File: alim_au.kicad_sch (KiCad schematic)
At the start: 34 parts, among them U1 AMS1117-3.3

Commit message: Correction orientation conn alim
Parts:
- C1, C?: LCSC (none) -> C440198
- C2: LCSC (none) -> C1588
- C?: LCSC (none) -> C45783
- C? (x2): LCSC (none) -> C14663
- C?: LCSC (none) -> C1620
- D20, D?: LCSC (none) -> C2286
- D? (x2): JLCPCB C191023 -> (none); LCSC (none) -> C191023
- D?: LCSC (none) -> C330388
- D?: LCSC (none) -> C603316
- Q? (x2): LCSC (none) -> C20917
- Q?: LCSC (none) -> C435954
- R30, R?: LCSC (none) -> C23162
- R34, R? (x5): LCSC (none) -> C25804
- R? (x2): LCSC (none) -> C25803
- R?: LCSC (none) -> C185324
- U1: LCSC (none) -> C7376
- U?: LCSC (none) -> C473914

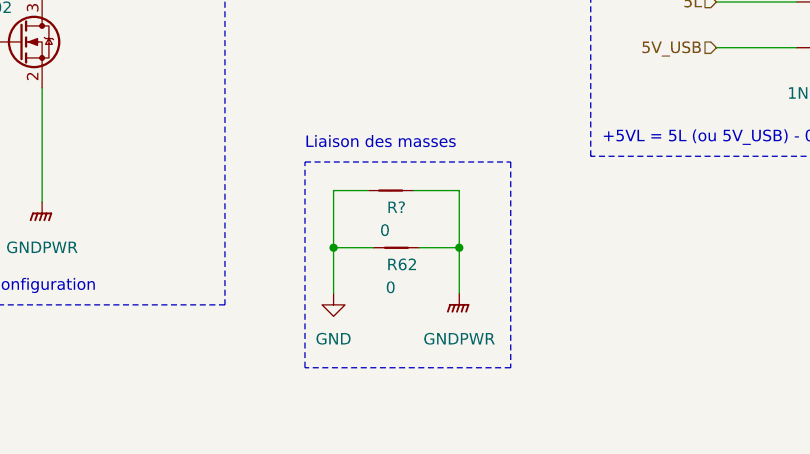
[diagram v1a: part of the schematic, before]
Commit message: added generic JLCPCB switch for reset and gnd netTie
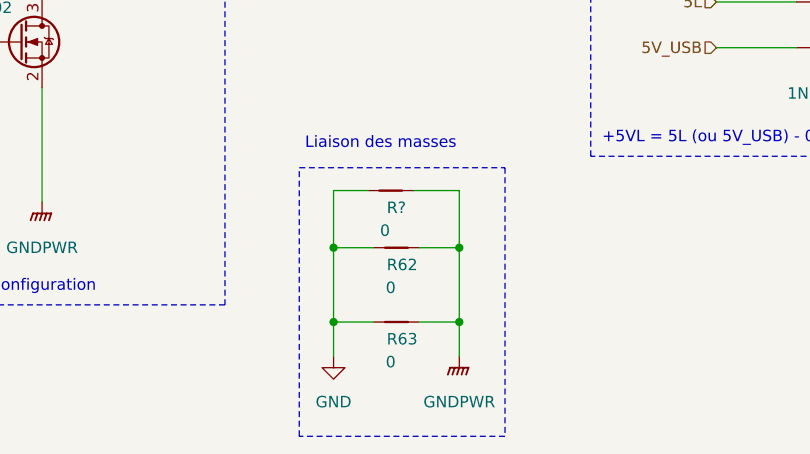
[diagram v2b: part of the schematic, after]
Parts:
- added R63: 0, NetTie:NetTie-2_SMD_Pad0.5mm, symbol Device:NetTie_2
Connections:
- net GND: now also R63.2
- net GNDPWR: now also R63.1
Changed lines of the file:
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@@
 	)
 	(junction
+		(at 124.46 162.56)
+		(diameter 0)
+		(color 0 0 0 0)
+	)
+	(junction
 		(at 126.365 67.31)
 		(diameter 0)
@@
 	)
 	(junction
+		(at 138.43 162.56)
+		(diameter 0)
+		(color 0 0 0 0)
+	)
+	(junction
 		(at 238.125 135.255)
 		(diameter 0)
@@
 	(wire
 		(pts
-			(xy 124.46 154.305) (xy 124.46 159.385)
+			(xy 124.46 154.305) (xy 124.46 162.56)
 		)
 		(stroke
@@
 	(wire
 		(pts
+			(xy 138.43 162.56) (xy 138.43 166.37)
+		)
+		(stroke
+			(width 0.5)
+			(type default)
+			(color 0 0 0 1)
+		)
+	)
+	(wire
+		(pts
 			(xy 243.84 60.325) (xy 250.825 60.325)
 		)
@@
 	(wire
 		(pts
+			(xy 124.46 162.56) (xy 128.905 162.56)
+		)
+		(stroke
+			(width 0)
+			(type default)
+		)
+	)
+	(wire
+		(pts
 			(xy 66.04 63.5) (xy 66.04 67.31)
 		)
@@
 	(wire
 		(pts
+			(xy 133.985 162.56) (xy 138.43 162.56)
+		)
+		(stroke
+			(width 0.5)
+			(type default)
+			(color 0 0 0 1)
+		)
+	)
+	(wire
+		(pts
 			(xy 80.645 77.47) (xy 70.485 77.47)
 		)
@@
 	(wire
 		(pts
+			(xy 124.46 162.56) (xy 124.46 166.37)
+		)
+		(stroke
+			(width 0)
+			(type default)
+		)
+	)
+	(wire
+		(pts
 			(xy 126.365 67.31) (xy 126.365 71.12)
 		)
@@
 	(wire
 		(pts
-			(xy 138.43 154.305) (xy 138.43 159.385)
+			(xy 138.43 154.305) (xy 138.43 162.56)
 		)
 		(stroke
@@
 	)
 	(rectangle
-		(start 121.285 144.78)
-		(end 144.145 167.64)
+		(start 120.65 145.415)
+		(end 143.51 175.26)
 		(stroke
 			(width 0)
@@
 	(symbol
 		(lib_id "power:GNDPWR")
-		(at 138.43 159.385 0)
+		(at 138.43 166.37 0)
 		(unit 1)
 		(exclude_from_sim no)
@@
 		(dnp no)
 		(property "Reference" "#PWR73"
-			(at 138.43 164.465 0)
+			(at 138.43 171.45 0)
 			(effects
 				(font
@@
 		)
 		(property "Value" "GNDPWR"
-			(at 138.43 164.465 0)
+			(at 138.43 171.45 0)
 			(effects
 				(font
@@
 		)
 		(property "Footprint" ""
-			(at 138.43 160.655 0)
+			(at 138.43 167.64 0)
 			(effects
 				(font
@@
 		)
 		(property "Datasheet" ""
-			(at 138.43 160.655 0)
+			(at 138.43 167.64 0)
 			(effects
 				(font
@@
 		)
 		(property "Description" ""
-			(at 138.43 159.385 0)
+			(at 138.43 166.37 0)
 			(effects
 				(font
@@
 	(symbol
 		(lib_id "power:GND")
-		(at 124.46 159.385 0)
+		(at 124.46 166.37 0)
 		(unit 1)
 		(exclude_from_sim no)
@@
 		(fields_autoplaced yes)
 		(property "Reference" "#PWR56"
-			(at 124.46 165.735 0)
+			(at 124.46 172.72 0)
 			(effects
 				(font
@@
 		)
 		(property "Value" "GND"
-			(at 124.46 164.465 0)
+			(at 124.46 171.45 0)
 			(effects
 				(font
@@
 		)
 		(property "Footprint" ""
-			(at 124.46 159.385 0)
+			(at 124.46 166.37 0)
 			(effects
 				(font
@@
 		)
 		(property "Datasheet" ""
-			(at 124.46 159.385 0)
+			(at 124.46 166.37 0)
 			(effects
 				(font
@@
 		)
 		(property "Description" ""
-			(at 124.46 159.385 0)
+			(at 124.46 166.37 0)
 			(effects
 				(font
@@
 					(unit 1)
 				)
+			)
+		)
+	)
+	(symbol
+		(lib_id "Device:NetTie_2")
+		(at 131.445 162.56 180)
+		(unit 1)
+		(exclude_from_sim no)
+		(in_bom no)
+		(on_board yes)
+		(dnp no)
+		(property "Reference" "R63"
+			(at 132.08 164.465 0)
+			(effects
+				(font
+					(size 1.27 1.27)
+				)
+			)
+		)
+		(property "Value" "0"
+			(at 130.81 167.005 0)
+			(effects
+				(font
+					(size 1.27 1.27)
+				)
+			)
+		)
+		(property "Footprint" "NetTie:NetTie-2_SMD_Pad0.5mm"
+			(at 131.445 162.56 0)
+			(effects
+				(font
+					(size 1.27 1.27)
+				)
+				(hide yes)
+			)
+		)
+		(property "Datasheet" "~"
+			(at 131.445 162.56 0)
+			(effects
+				(font
+					(size 1.27 1.27)
+				)
+				(hide yes)
+			)
+		)
+		(property "Description" "Net tie, 2 pins"
+			(at 131.445 162.56 0)
+			(effects
+				(font
+					(size 1.27 1.27)
+				)
+				(hide yes)
+			)
+		)
+		(pin "1"
+		)
+		(pin "2"
+		)
+		(instances
+			(project "12v-actuators-pcb"
+				(path "/d0b6cc72-ff07-4f5e-a148-04b65c86a715/a9998e65-7bac-4337-98c8-7de7c845405f"
+					(reference "R63")
+					(unit 1)
+				)

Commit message: corrrection footprint trim, ajout R64, config JLCPCB ASSY, fin panelisation (TODO: revue et cmd)
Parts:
- added R64: 13k, Resistor_SMD:R_0603_1608Metric, symbol Device:R_Small
- R?: value 523k -> 510k; LCSC C185324 -> C23192
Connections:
- net at R?.2, U?.6 (FB): now also R64.1; no longer R?.1
- new net: R64.2, R?.1
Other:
- moved on the sheet: R?
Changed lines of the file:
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@@
 	(wire
 		(pts
-			(xy 227.965 60.325) (xy 227.965 65.405)
+			(xy 227.965 60.325) (xy 227.965 61.595)
 		)
 		(stroke
@@
 	(wire
 		(pts
-			(xy 227.965 70.485) (xy 227.965 74.295)
+			(xy 227.965 66.675) (xy 227.965 67.31)
 		)
 		(stroke
@@
 	(wire
 		(pts
+			(xy 227.965 72.39) (xy 227.965 74.295)
+		)
+		(stroke
+			(width 0)
+			(type default)
+		)
+	)
+	(wire
+		(pts
 			(xy 89.535 76.2) (xy 89.535 77.47)
 		)
@@
 	(symbol
 		(lib_id "Device:R_Small")
-		(at 227.965 67.945 180)
+		(at 227.965 64.135 180)
 		(unit 1)
 		(exclude_from_sim no)
@@
 		(fields_autoplaced yes)
 		(property "Reference" "R?"
-			(at 230.505 67.31 0)
+			(at 230.505 63.5 0)
 			(effects
 				(font
@@
 			)
 		)
-		(property "Value" "523k"
-			(at 230.505 69.85 0)
+		(property "Value" "510k"
+			(at 230.505 66.04 0)
 			(effects
 				(font
@@
 		)
 		(property "Footprint" "Resistor_SMD:R_0603_1608Metric"
-			(at 227.965 67.945 0)
+			(at 227.965 64.135 0)
 			(effects
 				(font
@@
 		)
 		(property "Datasheet" "~"
-			(at 227.965 67.945 0)
+			(at 227.965 64.135 0)
 			(effects
 				(font
@@
 		)
 		(property "Description" ""
-			(at 227.965 67.945 0)
+			(at 227.965 64.135 0)
 			(effects
 				(font
@@
 			)
 		)
-		(property "LCSC" "C185324"
-			(at 227.965 67.945 0)
+		(property "LCSC" "C23192"
+			(at 227.965 64.135 0)
 			(effects
 				(font
@@
 					(unit 1)
 				)
+			)
+		)
+	)
+	(symbol
+		(lib_id "Device:R_Small")
+		(at 227.965 69.85 180)
+		(unit 1)
+		(exclude_from_sim no)
+		(in_bom yes)
+		(on_board yes)
+		(dnp no)
+		(fields_autoplaced yes)
+		(property "Reference" "R64"
+			(at 229.87 68.5799 0)
+			(effects
+				(font
+					(size 1.27 1.27)
+				)
+				(justify right)
+			)
+		)
+		(property "Value" "13k"
+			(at 229.87 71.1199 0)
+			(effects
+				(font
+					(size 1.27 1.27)
+				)
+				(justify right)
+			)
+		)
+		(property "Footprint" "Resistor_SMD:R_0603_1608Metric"
+			(at 227.965 69.85 0)
+			(effects
+				(font
+					(size 1.27 1.27)
+				)
+				(hide yes)
+			)
+		)
+		(property "Datasheet" "~"
+			(at 227.965 69.85 0)
+			(effects
+				(font
+					(size 1.27 1.27)
+				)
+				(hide yes)
+			)
+		)
+		(property "Description" ""
+			(at 227.965 69.85 0)
+			(effects
+				(font
+					(size 1.27 1.27)
+				)
+				(hide yes)
+			)
+		)
+		(property "LCSC" "C22797"
+			(at 227.965 69.85 0)
+			(effects
+				(font
+					(size 1.27 1.27)
+				)
+				(hide yes)
+			)
+		)
+		(pin "1"
+		)
+		(pin "2"
+		)
+		(instances
+			(project "12v-actuators-pcb"
+				(path "/d0b6cc72-ff07-4f5e-a148-04b65c86a715/a9998e65-7bac-4337-98c8-7de7c845405f"
+					(reference "R64")
+					(unit 1)
+				)

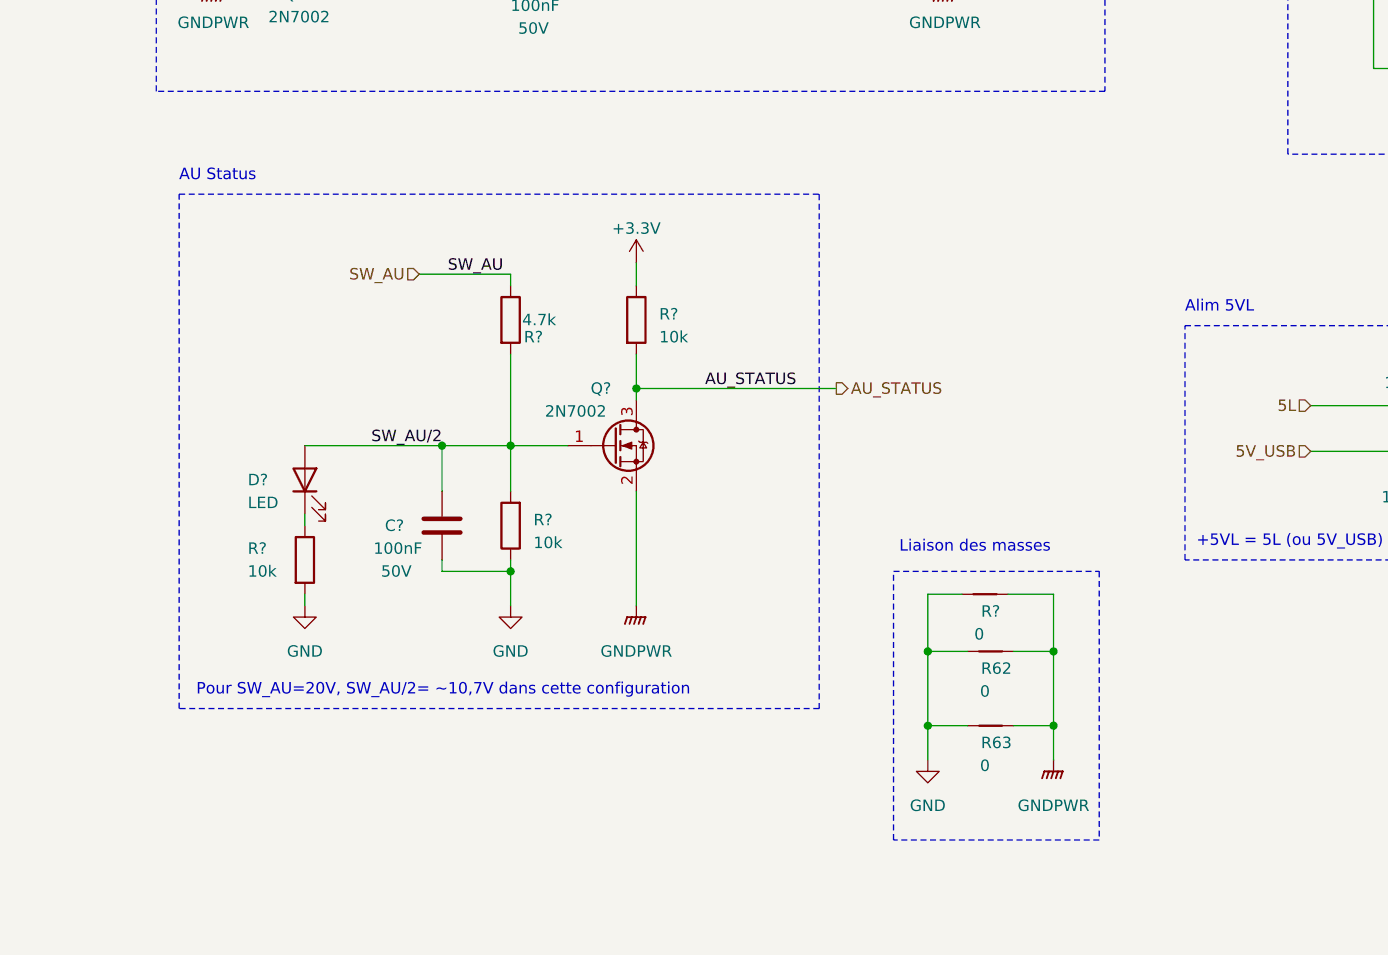
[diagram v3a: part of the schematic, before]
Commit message: mise à jour du schema après la coupe de belgique
- modification du circuit d'AU (SW_AU 24V->3.3V)
- modification du pinout de J3: ajout du CAN (suppression de J8) et du RST_EXT
- ajout d'un circuit de reset externe (configurable via 3-jumper)
- ajout d'un connecteur dédié pour un bouton reset externe
- ajout d'un debounce sur le switch reset
- mise à jour du routage et serigraphie
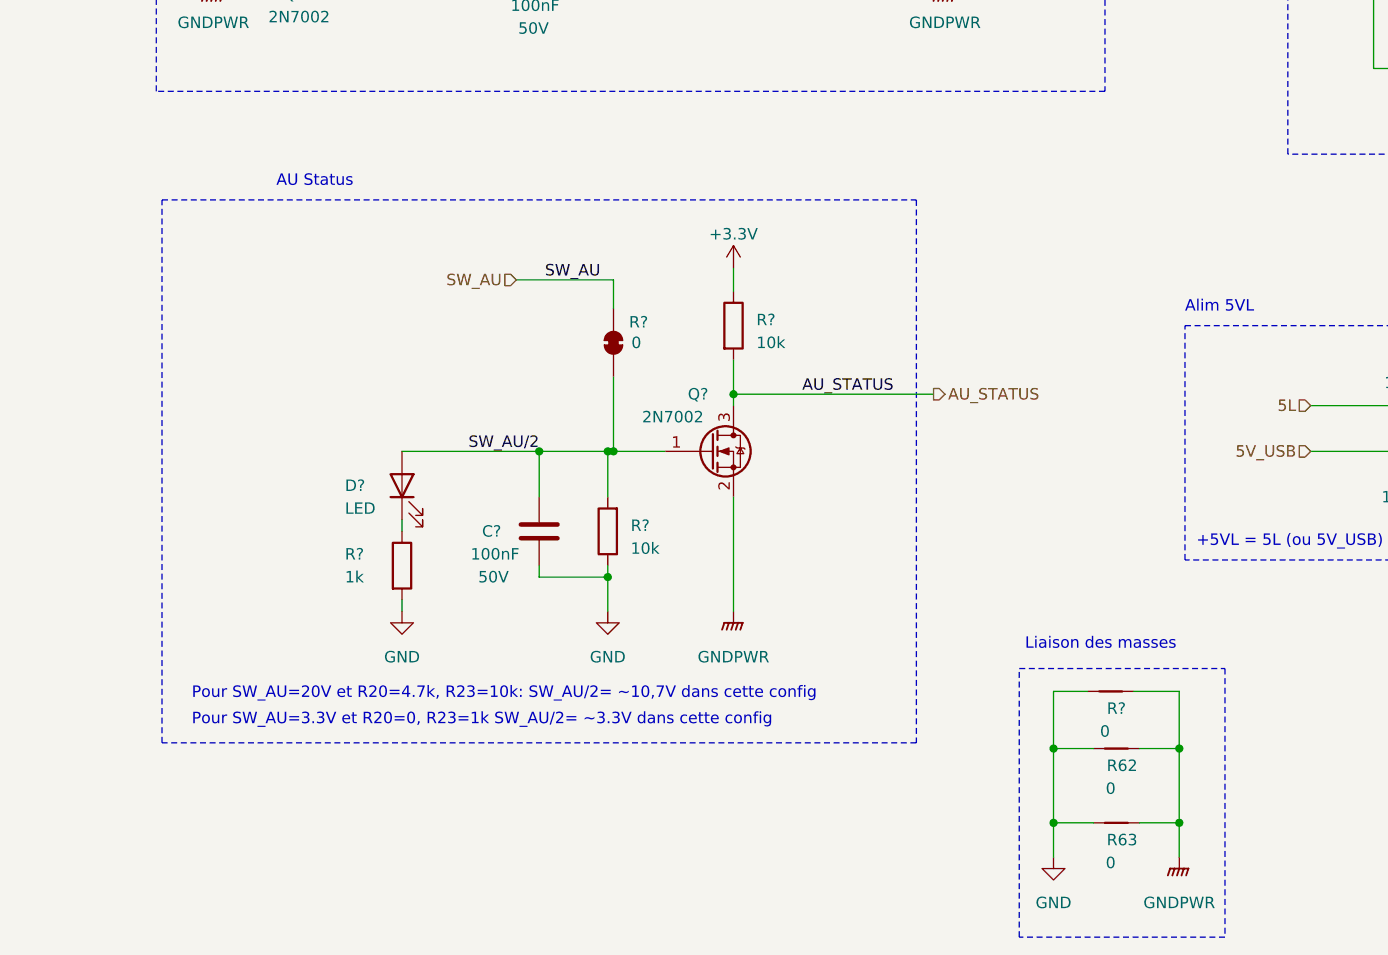
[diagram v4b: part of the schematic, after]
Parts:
- R?: value 4.7k -> 0; footprint Resistor_SMD:R_0603_1608Metric -> 12V-actuators_pcb:R_0402_1005Metric_jumperClosed; symbol Device:R -> Jumper:SolderJumper_2_Bridged; now left out of the parts list
- R?: value 10k -> 1k; LCSC C25804 -> C21190
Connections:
- net SW_AU: now also R?.2 (B); no longer R?.1
- net SW_AU/2: now also R?.1 (A); no longer R?.2
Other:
- note added: "Pour SW_AU=20V et R20=4.7k, R23=10k: SW_AU/2= ~10,7V dans cette config"
- note added: "Pour SW_AU=3.3V et R20=0, R23=1k SW_AU/2= ~3.3V dans cette config"
- note removed: "Pour SW_AU=20V, SW_AU/2= ~10,7V dans cette configuration"
- moved on the sheet: C?, D?, Q?, R62, R63, R?
